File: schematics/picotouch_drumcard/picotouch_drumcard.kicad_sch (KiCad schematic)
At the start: 73 parts, among them J1 AudioJack4, J2 AudioJack4, J3 AudioJack4, SW1 Capacitive Button, SW10 Capacitive Button, SW11 Capacitive Button, SW12 Capacitive Button, SW13 Capacitive Button, SW14 Capacitive Button, SW15 Capacitive Button, SW16 Capacitive Button, SW17 Capacitive Button, SW2 Capacitive Button, SW3 Capacitive Button, SW4 Capacitive Button, SW5 Capacitive Button, SW6 Capacitive Button, SW7 Capacitive Button, SW8 Capacitive Button, SW9 Capacitive Button, U1 Pico, U2 H11L1S(TA), U3 MCP73831-2-OT, U4 TS20, X1 AFC20-S02ACA-00

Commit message: second
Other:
- moved on the sheet: J2, J3
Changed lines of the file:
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@@
 	)
 	(no_connect
-		(at 93.98 68.58)
+		(at 93.98 86.36)
 	)
 	(no_connect
@@
 	)
 	(no_connect
-		(at 77.47 71.12)
+		(at 91.44 134.62)
 	)
 	(no_connect
-		(at 93.98 73.66)
+		(at 77.47 71.12)
 	)
 	(no_connect
@@
 	)
 	(no_connect
+		(at 91.44 165.1)
+	)
+	(no_connect
 		(at 157.48 153.67)
 	)
@@
 	)
 	(no_connect
-		(at 93.98 66.04)
-	)
-	(no_connect
 		(at 157.48 156.21)
 	)
@@
 	(wire
 		(pts
-			(xy 83.312 154.94) (xy 73.66 154.94)
+			(xy 82.55 154.94) (xy 73.66 154.94)
 		)
 		(stroke
@@
 	(wire
 		(pts
-			(xy 92.202 167.64) (xy 88.392 167.64)
-		)
-		(stroke
-			(width 0)
-			(type default)
-		)
-	)
-	(wire
-		(pts
 			(xy 87.63 132.08) (xy 87.63 129.54)
 		)
@@
 	(wire
 		(pts
-			(xy 92.71 129.54) (xy 87.63 129.54)
+			(xy 91.44 129.54) (xy 87.63 129.54)
 		)
 		(stroke
@@
 	(wire
 		(pts
-			(xy 83.312 162.56) (xy 83.312 154.94)
+			(xy 82.55 162.56) (xy 82.55 154.94)
 		)
 		(stroke
@@
 	(wire
 		(pts
-			(xy 90.17 137.16) (xy 92.71 137.16)
+			(xy 90.17 137.16) (xy 91.44 137.16)
 		)
 		(stroke
@@
 	(wire
 		(pts
-			(xy 92.71 132.08) (xy 87.63 132.08)
+			(xy 91.44 132.08) (xy 87.63 132.08)
 		)
 		(stroke
@@
 	(wire
 		(pts
-			(xy 148.59 118.11) (xy 157.48 118.11)
+			(xy 73.66 160.02) (xy 91.44 160.02)
 		)
 		(stroke
@@
 	(wire
 		(pts
-			(xy 91.44 181.61) (xy 82.55 181.61)
+			(xy 148.59 118.11) (xy 157.48 118.11)
 		)
 		(stroke
@@
 	(wire
 		(pts
-			(xy 135.89 163.83) (xy 135.89 166.37)
+			(xy 91.44 181.61) (xy 82.55 181.61)
 		)
 		(stroke
@@
 	(wire
 		(pts
-			(xy 99.06 113.03) (xy 123.19 113.03)
+			(xy 135.89 163.83) (xy 135.89 166.37)
 		)
 		(stroke
@@
 	(wire
 		(pts
-			(xy 105.41 115.57) (xy 123.19 115.57)
+			(xy 99.06 113.03) (xy 123.19 113.03)
 		)
 		(stroke
@@
 	(wire
 		(pts
-			(xy 236.22 24.13) (xy 246.38 24.13)
+			(xy 105.41 115.57) (xy 123.19 115.57)
 		)
 		(stroke
@@
 	(wire
 		(pts
-			(xy 148.59 140.97) (xy 157.48 140.97)
+			(xy 236.22 24.13) (xy 246.38 24.13)
 		)
 		(stroke
@@
 	(wire
 		(pts
-			(xy 92.202 162.56) (xy 83.312 162.56)
+			(xy 148.59 140.97) (xy 157.48 140.97)
 		)
 		(stroke
@@
 	(wire
 		(pts
+			(xy 86.36 167.64) (xy 91.44 167.64)
+		)
+		(stroke
+			(width 0)
+			(type default)
+		)
+	)
+	(wire
+		(pts
 			(xy 99.06 110.49) (xy 99.06 113.03)
 		)
@@
 	(wire
 		(pts
-			(xy 236.22 91.44) (xy 246.38 91.44)
+			(xy 82.55 162.56) (xy 91.44 162.56)
 		)
 		(stroke
@@
 	(wire
 		(pts
-			(xy 29.21 93.98) (xy 41.91 93.98)
+			(xy 236.22 91.44) (xy 246.38 91.44)
 		)
 		(stroke
@@
 	(wire
 		(pts
-			(xy 38.1 152.4) (xy 38.1 154.94)
+			(xy 29.21 93.98) (xy 41.91 93.98)
 		)
 		(stroke
@@
 	(wire
 		(pts
-			(xy 92.202 160.02) (xy 73.66 160.02)
+			(xy 38.1 152.4) (xy 38.1 154.94)
 		)
 		(stroke
@@
 	(symbol
 		(lib_id "Connector_Audio:AudioJack4")
-		(at 97.282 165.1 180)
+		(at 96.52 165.1 180)
 		(unit 1)
 		(exclude_from_sim no)
@@
 		(fields_autoplaced yes)
 		(property "Reference" "J2"
-			(at 106.172 161.9249 0)
+			(at 105.41 161.9249 0)
 			(effects
 				(font
@@
 		)
 		(property "Value" "AudioJack4"
-			(at 106.172 164.4649 0)
+			(at 105.41 164.4649 0)
 			(effects
 				(font
@@
 		)
 		(property "Footprint" "todbot_stuff:Jack_3.5mm_PJ320D_Horizontal"
-			(at 97.282 165.1 0)
+			(at 96.52 165.1 0)
 			(effects
 				(font
@@
 		)
 		(property "Datasheet" "~"
-			(at 97.282 165.1 0)
+			(at 96.52 165.1 0)
 			(effects
 				(font
@@
 		)
 		(property "Description" "Audio Jack, 4 Poles (TRRS)"
-			(at 97.282 165.1 0)
+			(at 96.52 165.1 0)
 			(effects
 				(font
@@
 	(symbol
 		(lib_id "power:GND")
-		(at 88.392 167.64 0)
+		(at 86.36 167.64 0)
 		(mirror y)
 		(unit 1)
@@
 		(dnp no)
 		(property "Reference" "#PWR016"
-			(at 88.392 173.99 0)
+			(at 86.36 173.99 0)
 			(effects
 				(font
@@
 		)
 		(property "Value" "GND"
-			(at 84.582 169.418 0)
+			(at 82.55 169.418 0)
 			(effects
 				(font
@@
 		)
 		(property "Footprint" ""
-			(at 88.392 167.64 0)
+			(at 86.36 167.64 0)
 			(effects
 				(font
@@
 		)
 		(property "Datasheet" ""
-			(at 88.392 167.64 0)
+			(at 86.36 167.64 0)
 			(effects
 				(font
@@
 		)
 		(property "Description" "Power symbol creates a global label with name \"GND\" , ground"
-			(at 88.392 167.64 0)
+			(at 86.36 167.64 0)
 			(effects
 				(font
@@
 	(symbol
 		(lib_id "Connector_Audio:AudioJack4")
-		(at 97.79 134.62 180)
+		(at 96.52 134.62 180)
 		(unit 1)
 		(exclude_from_sim no)
@@
 		(fields_autoplaced yes)
 		(property "Reference" "J3"
-			(at 106.68 131.4449 0)
+			(at 105.41 131.4449 0)
 			(effects
 				(font
@@
 		)
 		(property "Value" "AudioJack4"
-			(at 106.68 133.9849 0)
+			(at 105.41 133.9849 0)
 			(effects
 				(font
@@
 		)
 		(property "Footprint" "todbot_stuff:Jack_3.5mm_PJ320D_Horizontal"
-			(at 97.79 134.62 0)
+			(at 96.52 134.62 0)
 			(effects
 				(font
@@
 		)
 		(property "Datasheet" "~"
-			(at 97.79 134.62 0)
+			(at 96.52 134.62 0)
 			(effects
 				(font
@@
 		)
 		(property "Description" "Audio Jack, 4 Poles (TRRS)"
-			(at 97.79 134.62 0)
+			(at 96.52 134.62 0)
 			(effects
 				(font

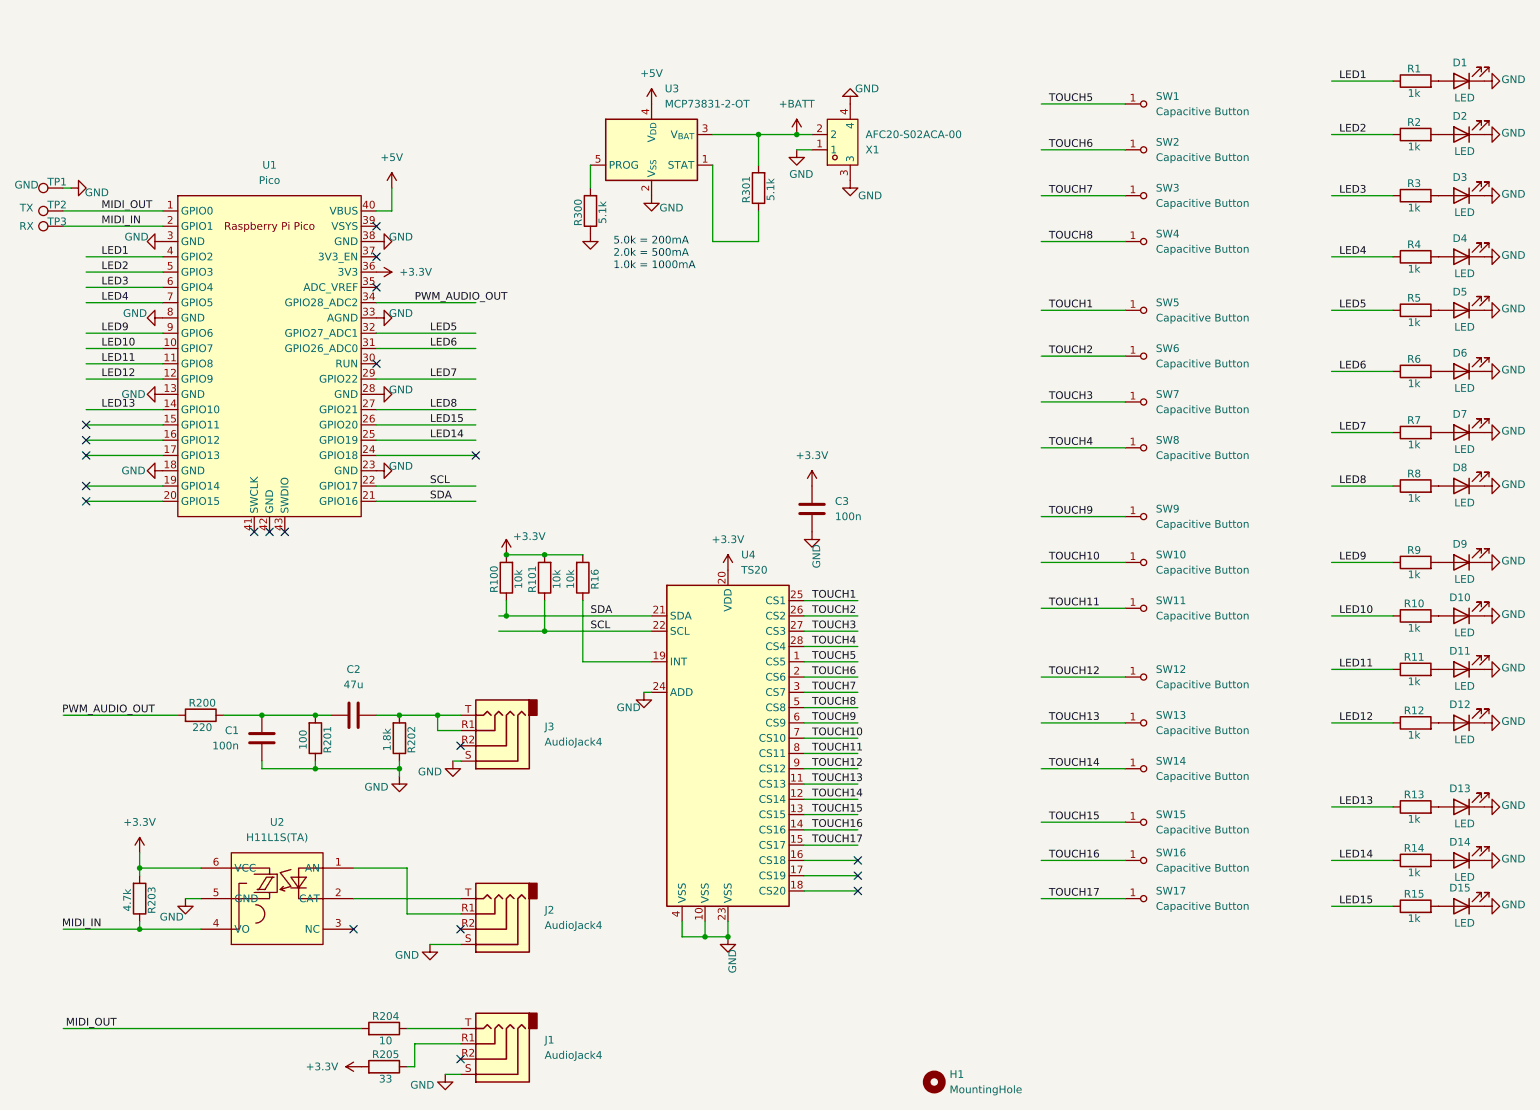
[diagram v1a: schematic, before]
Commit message: added protection diodes
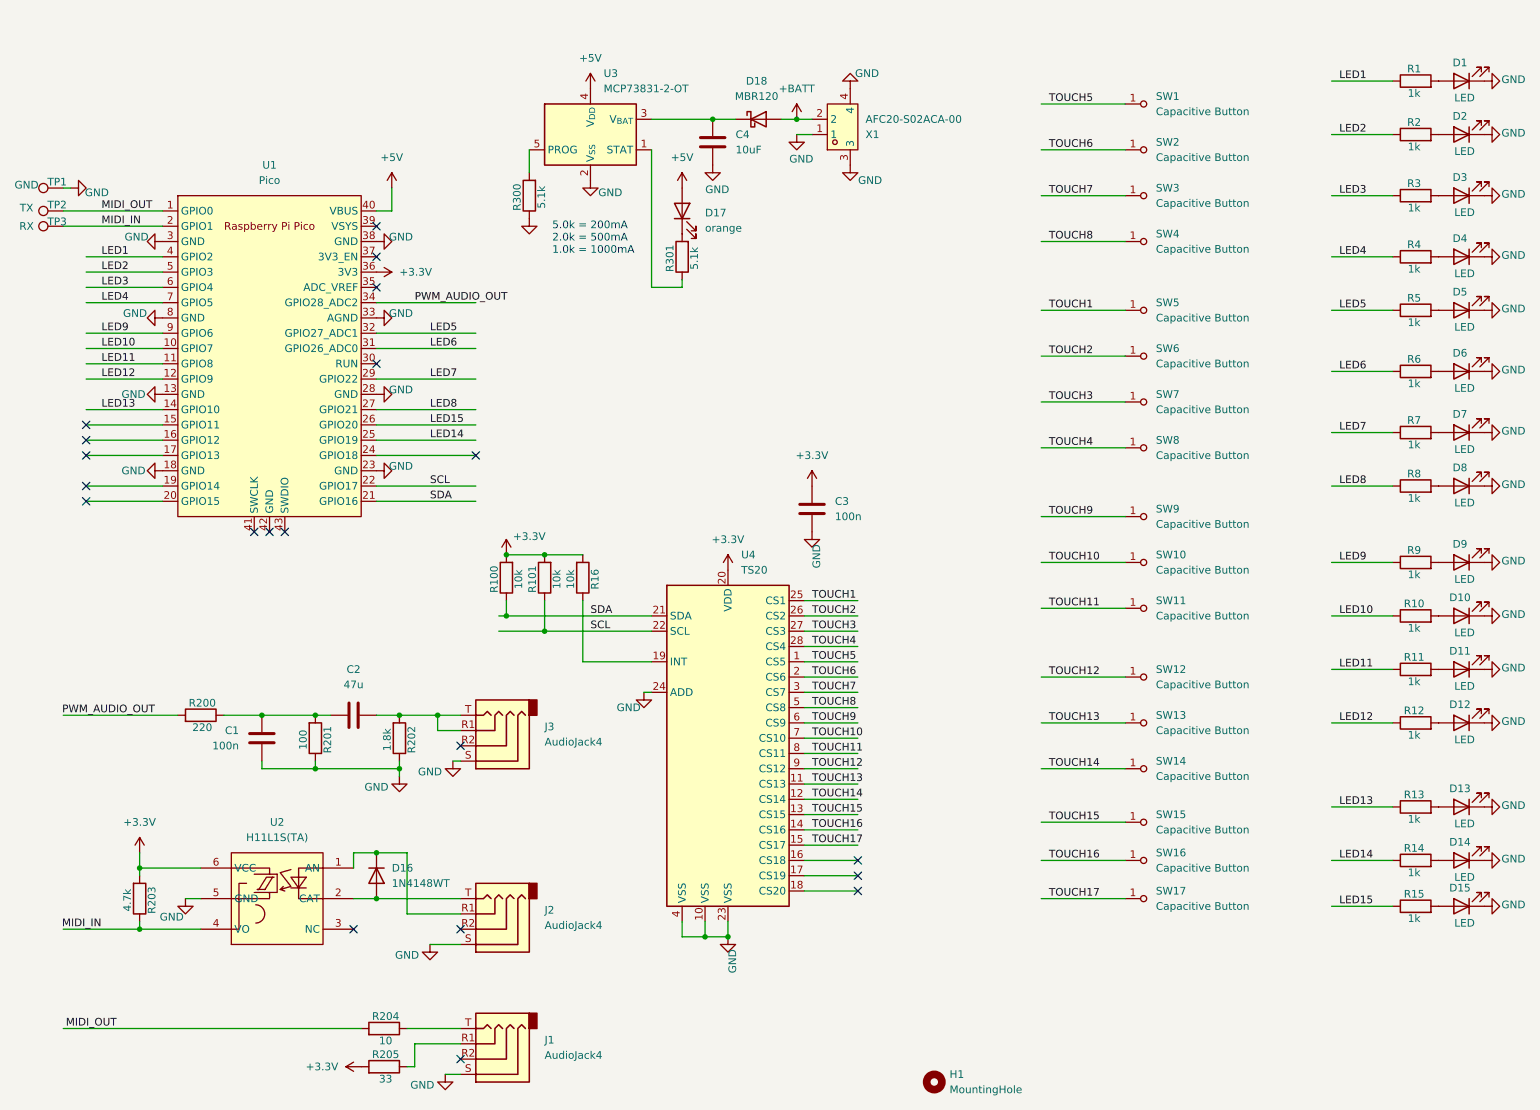
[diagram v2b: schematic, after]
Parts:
- added C4: 10uF, Capacitor_SMD:C_0603_1608Metric, symbol Device:C
- added D16: 1N4148WT, Diode_SMD:D_SOD-123F, symbol Diode:1N4148WT
- added D17: orange, LED_SMD:LED_0603_1608Metric, symbol Device:LED
- added D18: MBR120, Diode_SMD:D_SOD-123F, symbol Device:D_Schottky
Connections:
- net +5V: now also D17.2 (A)
- net +BATT: now also D18.2 (A); no longer R301.2, U3.3 (V_{BAT})
- net GND: now also C4.2
- net at J2.R1, U2.1 (AN): now also D16.1 (K)
- net at J2.T, U2.2 (CAT): now also D16.2 (A)
- new net: D17.1 (K), R301.2
- new net: C4.1, D18.1 (K), U3.3 (V_{BAT})
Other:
- moved on the sheet: R300, R301, U3, X1

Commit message: tuning layout
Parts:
- D16: LCSC Part (none) -> C64898
- D18: LCSC Part (none) -> C130880
- J1: LCSC (none) -> C431535
- J2, J3: LCSC Part (none) -> C431535
- U3: LCSC Part (none) -> C424093
- U4: LCSC Part (none) -> C95876
- renumbered R100 to R17, R101 to R18, R200 to R19, R201 to R20, R202 to R21, R203 to R22, R204 to R23, R205 to R24
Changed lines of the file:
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@@
 		(on_board yes)
 		(dnp no)
-		(property "Reference" "R200"
+		(property "Reference" "R19"
 			(at 48.514 127.508 90)
 			(effects
@@
 			(project "picotouch_drumcard"
 				(path "/5e315703-690d-40b0-a846-b905406b612c"
-					(reference "R200")
+					(reference "R19")
 					(unit 1)
 				)
@@
 			)
 		)
+		(property "LCSC Part" "C431535"
+			(at 96.52 165.1 0)
+			(effects
+				(font
+					(size 1.27 1.27)
+				)
+				(hide yes)
+			)
+		)
 		(pin "S"
 		)
@@
 			)
 		)
+		(property "LCSC Part" "C424093"
+			(at 113.03 33.02 0)
+			(effects
+				(font
+					(size 1.27 1.27)
+				)
+				(hide yes)
+			)
+		)
 		(pin "5"
 		)
@@
 		(on_board yes)
 		(dnp no)
-		(property "Reference" "R201"
+		(property "Reference" "R20"
 			(at 69.342 133.604 90)
 			(effects
@@
 			(project "picotouch_drumcard"
 				(path "/5e315703-690d-40b0-a846-b905406b612c"
-					(reference "R201")
+					(reference "R20")
 					(unit 1)
 				)
@@
 		(on_board yes)
 		(dnp no)
-		(property "Reference" "R203"
+		(property "Reference" "R22"
 			(at 40.132 160.274 90)
 			(effects
@@
 			(project "picotouch_drumcard"
 				(path "/5e315703-690d-40b0-a846-b905406b612c"
-					(reference "R203")
+					(reference "R22")
 					(unit 1)
 				)
@@
 			)
 		)
+		(property "LCSC Part" "C130880"
+			(at 140.97 30.48 0)
+			(effects
+				(font
+					(size 1.27 1.27)
+				)
+				(hide yes)
+			)
+		)
 		(pin "1"
 		)
@@
 			)
 		)
+		(property "LCSC Part" "C64898"
+			(at 77.47 156.21 90)
+			(effects
+				(font
+					(size 1.27 1.27)
+				)
+				(hide yes)
+			)
+		)
 		(pin "1"
 		)
@@
 			)
 		)
+		(property "LCSC Part" "C95876"
+			(at 135.89 134.62 0)
+			(effects
+				(font
+					(size 1.27 1.27)
+				)
+				(hide yes)
+			)
+		)
 		(pin "8"
 		)
@@
 		(on_board yes)
 		(dnp no)
-		(property "Reference" "R205"
+		(property "Reference" "R24"
 			(at 78.994 185.928 90)
 			(effects
@@
 			(project "picotouch_bizcard"
 				(path "/5e315703-690d-40b0-a846-b905406b612c"
-					(reference "R205")
+					(reference "R24")
 					(unit 1)
 				)
@@
 			)
 		)
+		(property "LCSC Part" "C431535"
+			(at 96.52 134.62 0)
+			(effects
+				(font
+					(size 1.27 1.27)
+				)
+				(hide yes)
+			)
+		)
 		(pin "S"
 		)
@@
 		(on_board yes)
 		(dnp no)
-		(property "Reference" "R101"
+		(property "Reference" "R18"
 			(at 103.378 106.934 90)
 			(effects
@@
 			(project "picotouch_drumcard"
 				(path "/5e315703-690d-40b0-a846-b905406b612c"
-					(reference "R101")
+					(reference "R18")
 					(unit 1)
 				)
@@
 		(on_board yes)
 		(dnp no)
-		(property "Reference" "R100"
+		(property "Reference" "R17"
 			(at 97.028 106.934 90)
 			(effects
@@
 			(project "picotouch_drumcard"
 				(path "/5e315703-690d-40b0-a846-b905406b612c"
-					(reference "R100")
+					(reference "R17")
 					(unit 1)
 				)
@@
 			)
 		)
+		(property "LCSC" "C431535"
+			(at 193.04 0 0)
+			(effects
+				(font
+					(size 1.27 1.27)
+				)
+				(hide yes)
+			)
+		)
 		(pin "S"
 		)
@@
 		(dnp no)
 		(property "Reference" "R16"
-			(at 113.792 106.934 90)
+			(at 109.728 106.934 90)
 			(effects
 				(font
@@
 		)
 		(property "Value" "10k"
-			(at 109.728 106.934 90)
+			(at 113.792 106.68 90)
 			(effects
 				(font
@@
 		(on_board yes)
 		(dnp no)
-		(property "Reference" "R204"
+		(property "Reference" "R23"
 			(at 78.994 179.578 90)
 			(effects
@@
 			(project "picotouch_bizcard"
 				(path "/5e315703-690d-40b0-a846-b905406b612c"
-					(reference "R204")
+					(reference "R23")
 					(unit 1)
 				)
@@
 		(on_board yes)
 		(dnp no)
-		(property "Reference" "R202"
+		(property "Reference" "R21"
 			(at 83.312 133.604 90)
 			(effects
@@
 			(project "picotouch_drumcard"
 				(path "/5e315703-690d-40b0-a846-b905406b612c"
-					(reference "R202")
+					(reference "R21")
 					(unit 1)
 				)
